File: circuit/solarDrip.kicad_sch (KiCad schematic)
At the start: 44 parts, among them J1 solar_charger, J10 Conn_01x08_Socket, J2 batt, J3 solar, J4 pump, J5 soil, J6 water, J7 USB_C_Receptacle_USB2.0_14P, J8 i2c, J9 Conn_01x08_Socket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

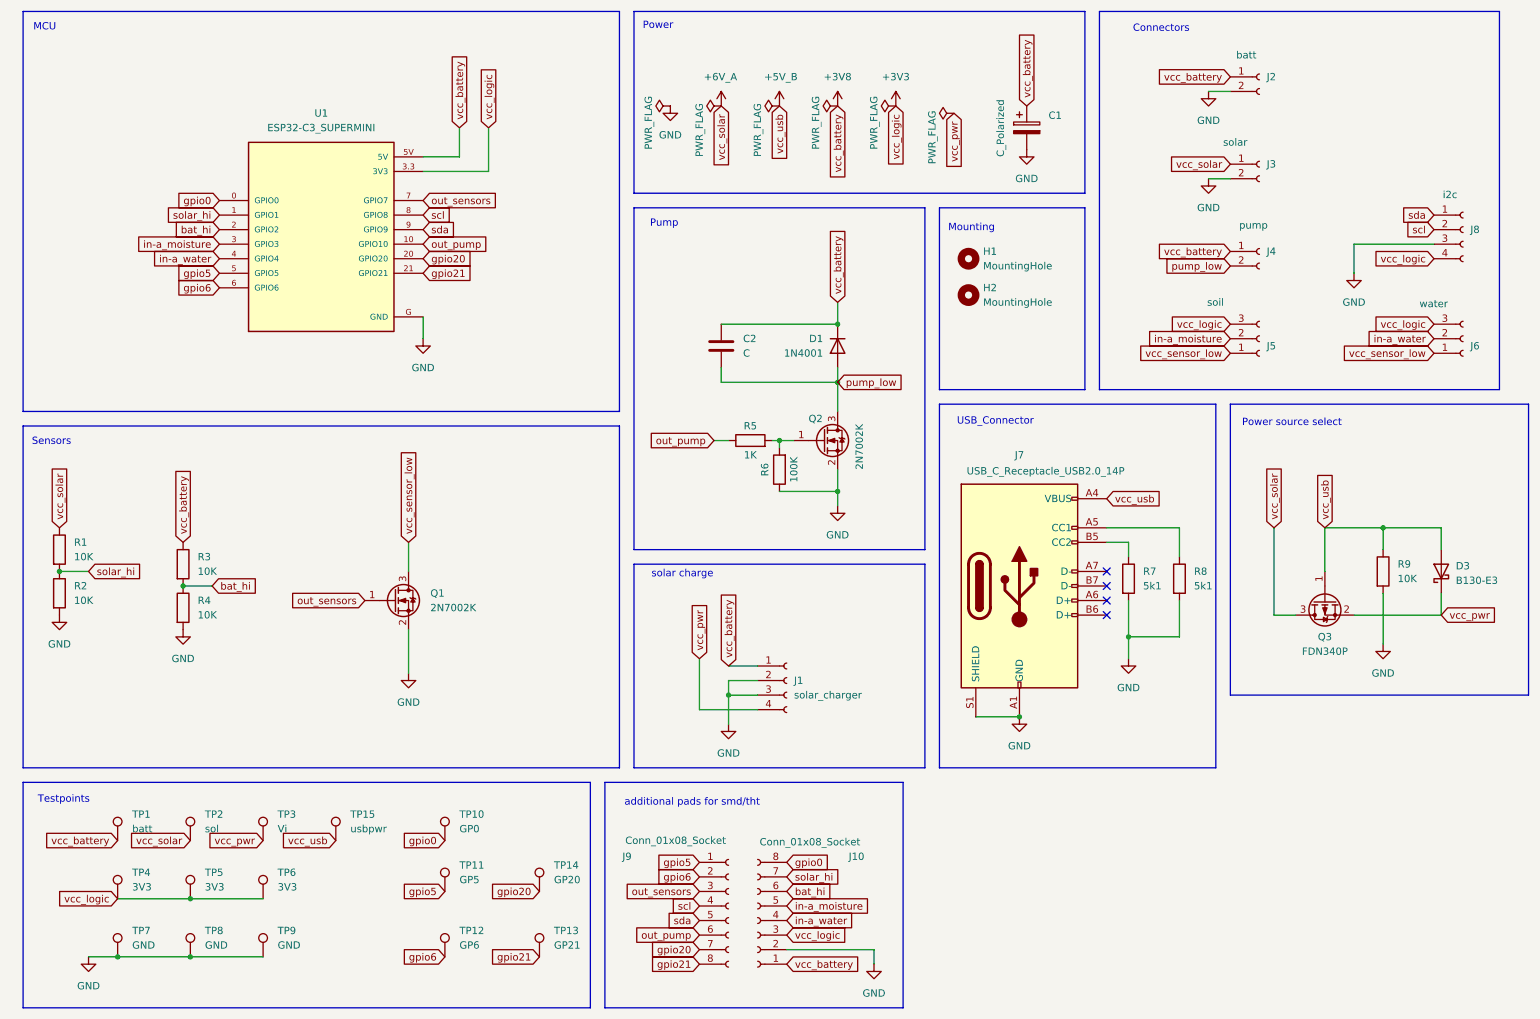
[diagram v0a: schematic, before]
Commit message: sch: add bypass caps to sensor pins
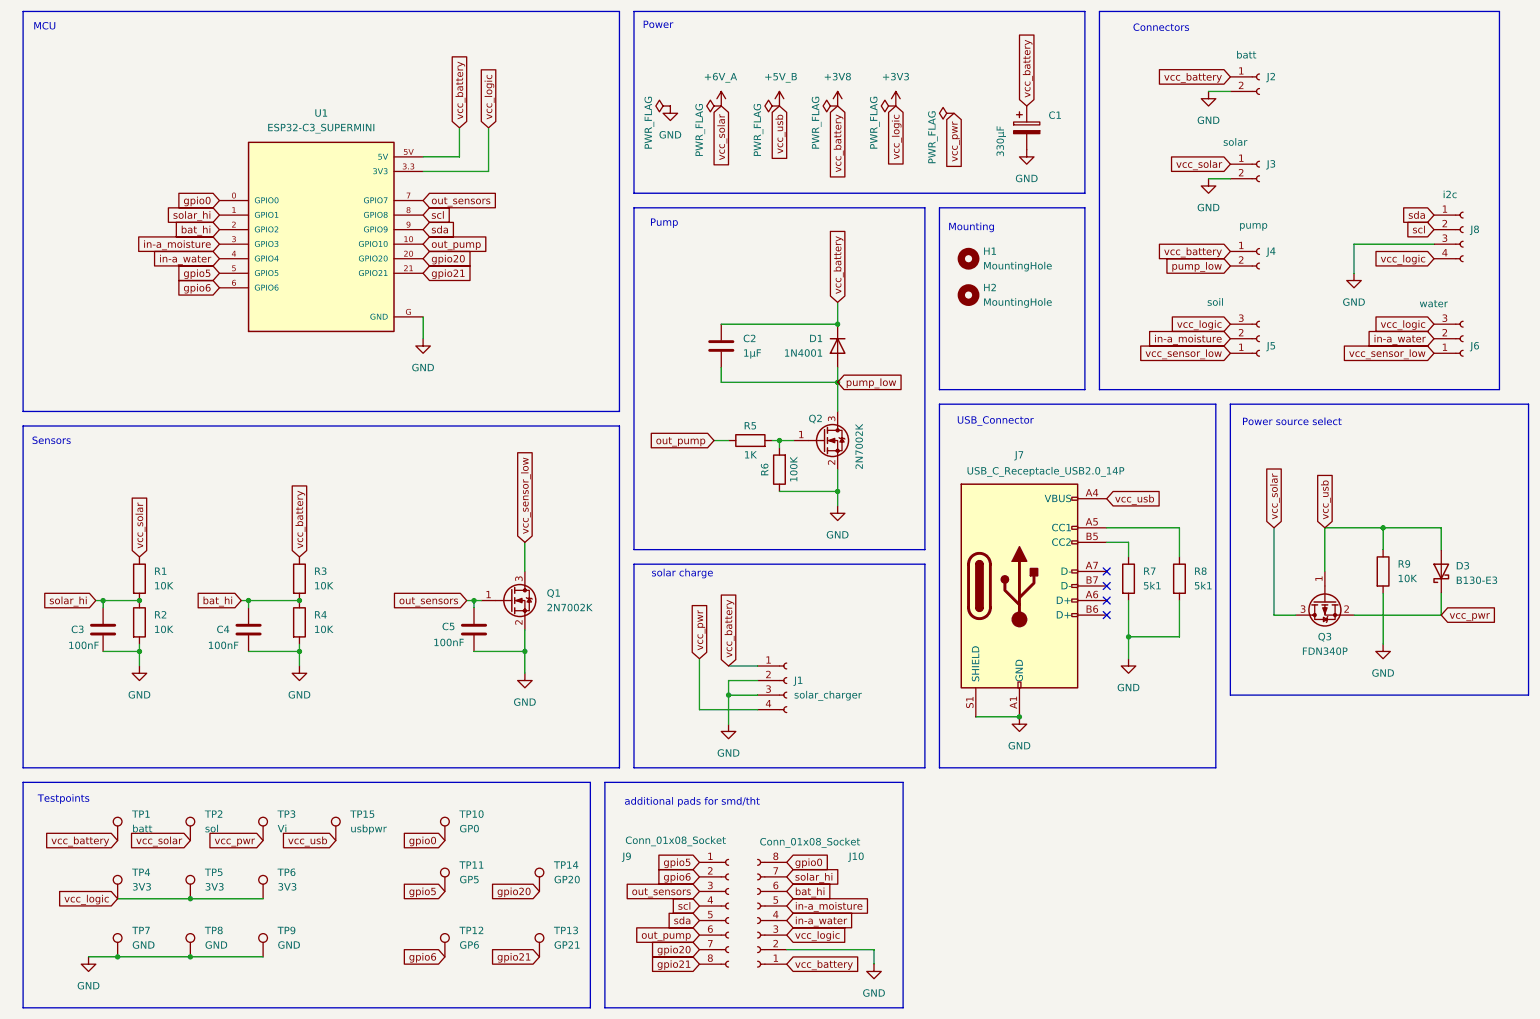
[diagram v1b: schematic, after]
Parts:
- added C3, C4, C5: 100nF, Capacitor_SMD:C_0504_1310Metric_Pad0.83x1.28mm_HandSolder, symbol Device:C
- C1: value C_Polarized -> 330µF
- C2: value C -> 1µF
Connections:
- net GND: now also C3.2, C4.2, C5.2
- net bat_hi: now also C4.1
- net out_sensors: now also C5.1
- net solar_hi: now also C3.1
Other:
- moved on the sheet: Q1, R1, R2, R3, R4

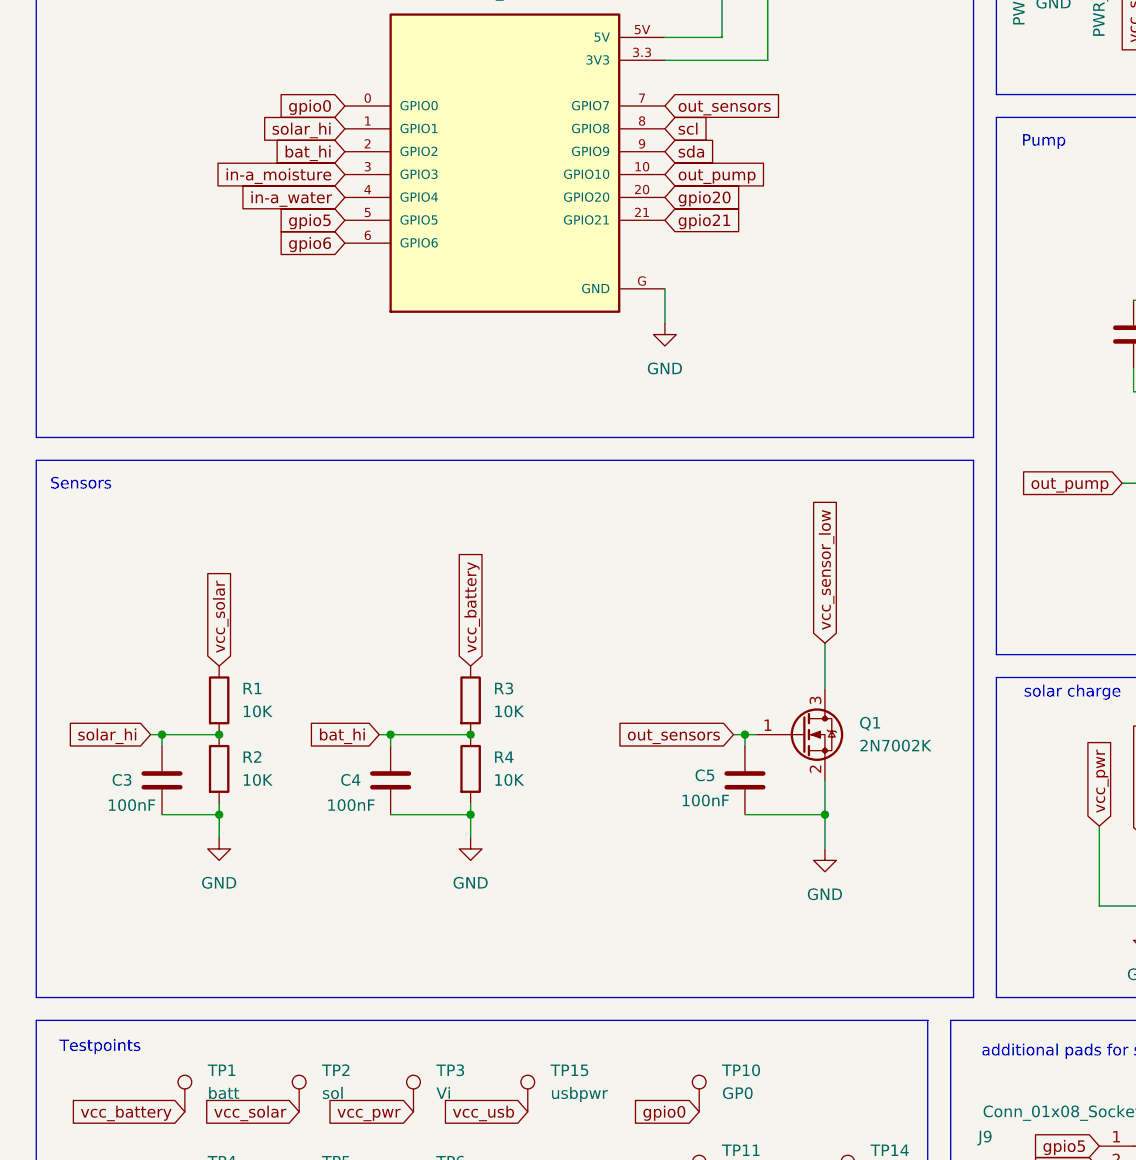
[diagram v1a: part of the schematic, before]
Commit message: add sensor pypass caps
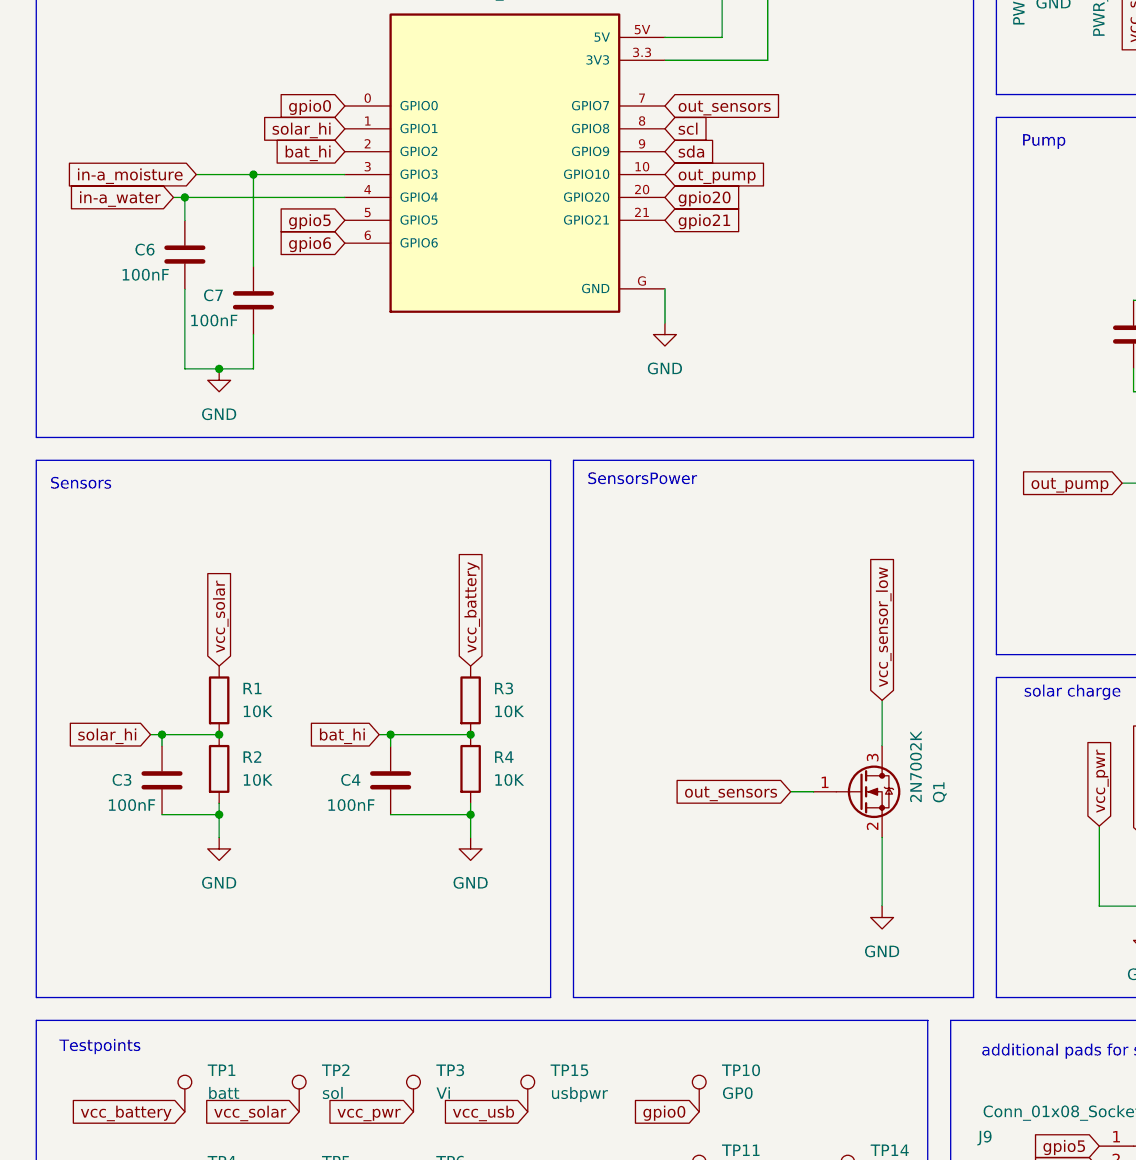
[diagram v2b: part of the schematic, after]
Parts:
- removed C5: 100nF, Capacitor_SMD:C_0504_1310Metric_Pad0.83x1.28mm_HandSolder, symbol Device:C
- added C6, C7: 100nF, Capacitor_SMD:C_0504_1310Metric_Pad0.83x1.28mm_HandSolder, symbol Device:C
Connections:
- net GND: now also C6.2, C7.2
- net in-a_moisture: now also C7.1
- net in-a_water: now also C6.1
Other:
- note added: "SensorsPower"
- moved on the sheet: Q1

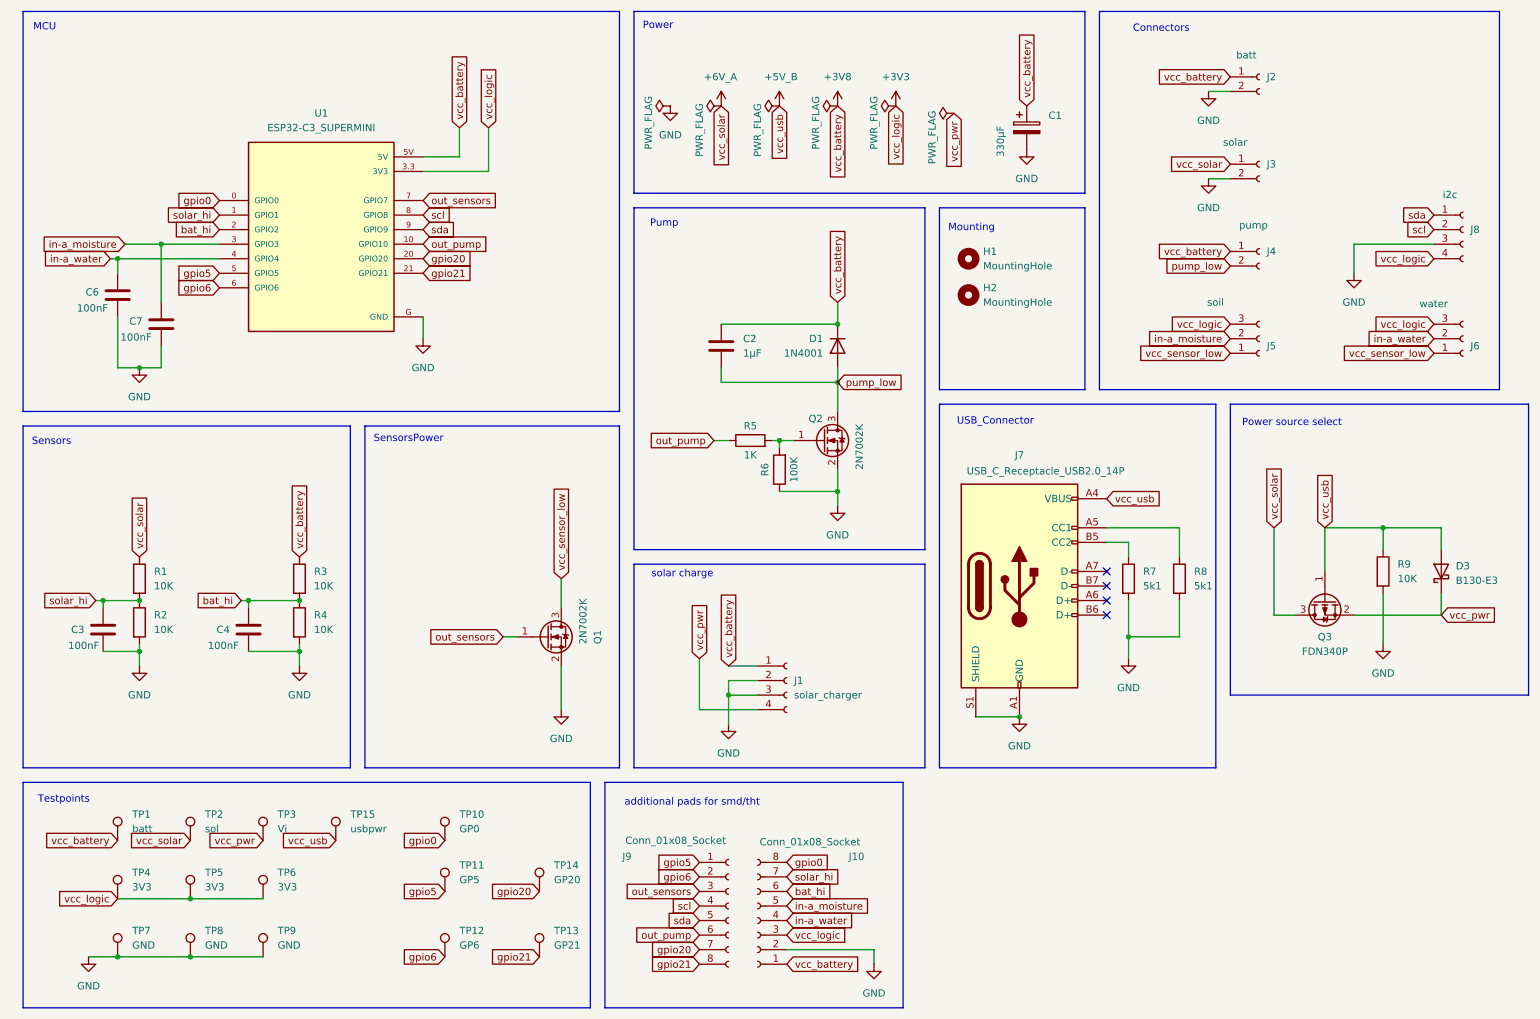
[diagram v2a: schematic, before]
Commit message: add artwork: dripbot & mc3 logo
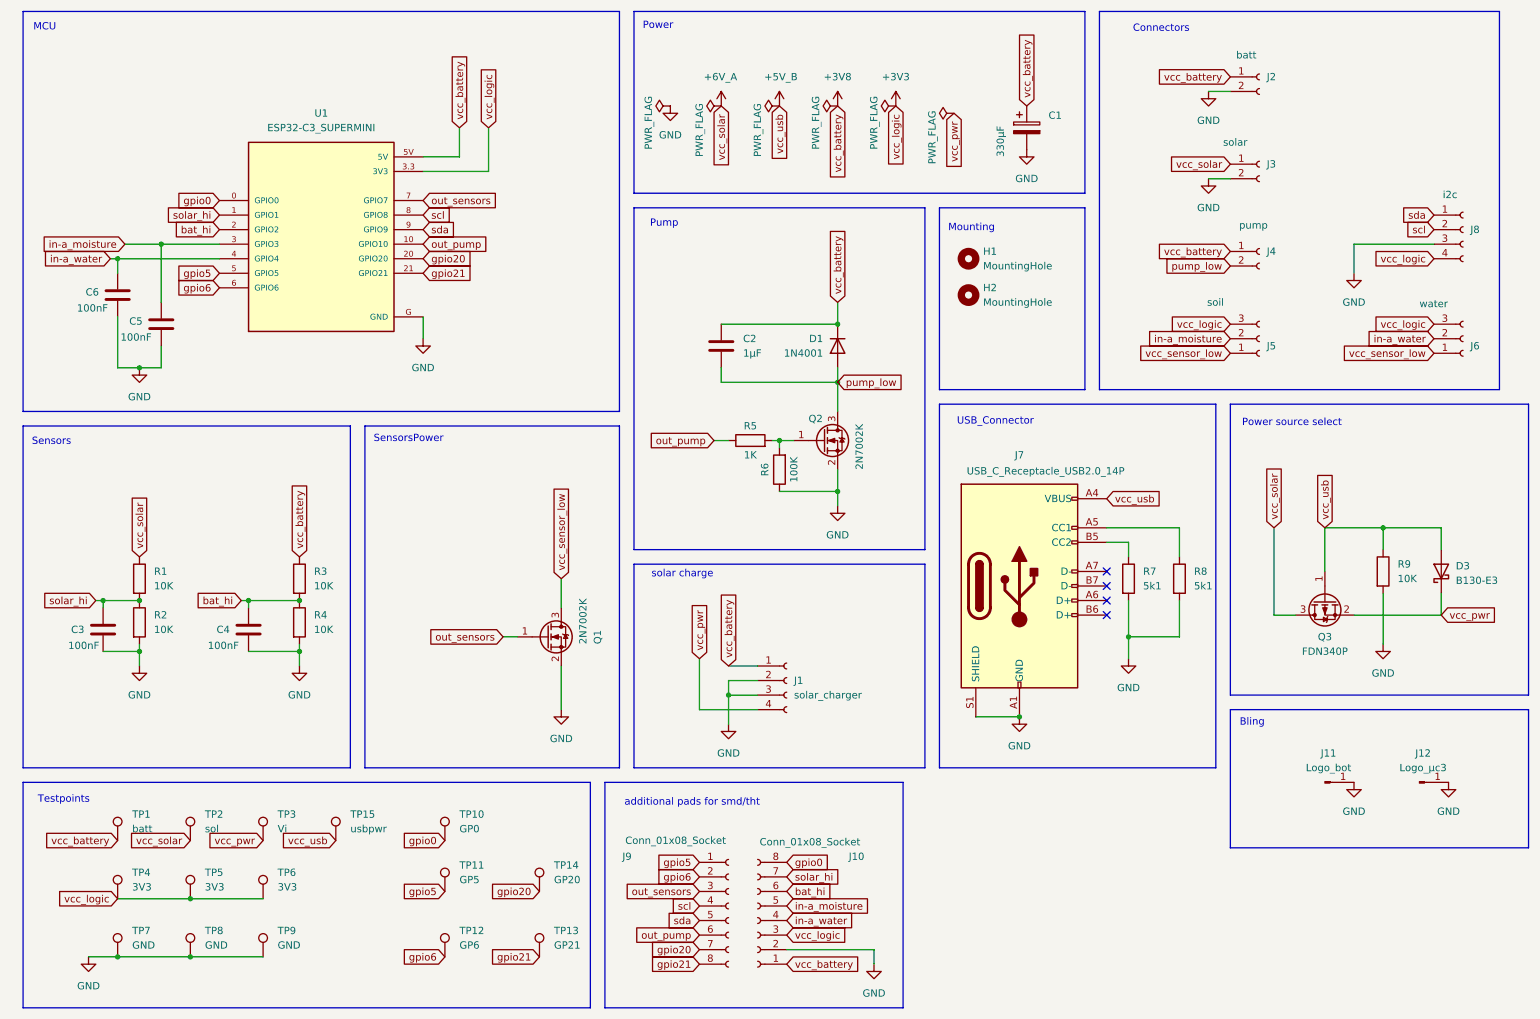
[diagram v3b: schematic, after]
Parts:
- added J11: Logo_bot, my_footprints:logo_solardrip, symbol Connector:Conn_01x01_Pin
- added J12: Logo_µc3, my_footprints:muccc_logo, symbol Connector:Conn_01x01_Pin
- renumbered C7 to C5
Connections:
- net GND: now also J11.1 (Pin_1), J12.1 (Pin_1)
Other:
- note added: "Bling"

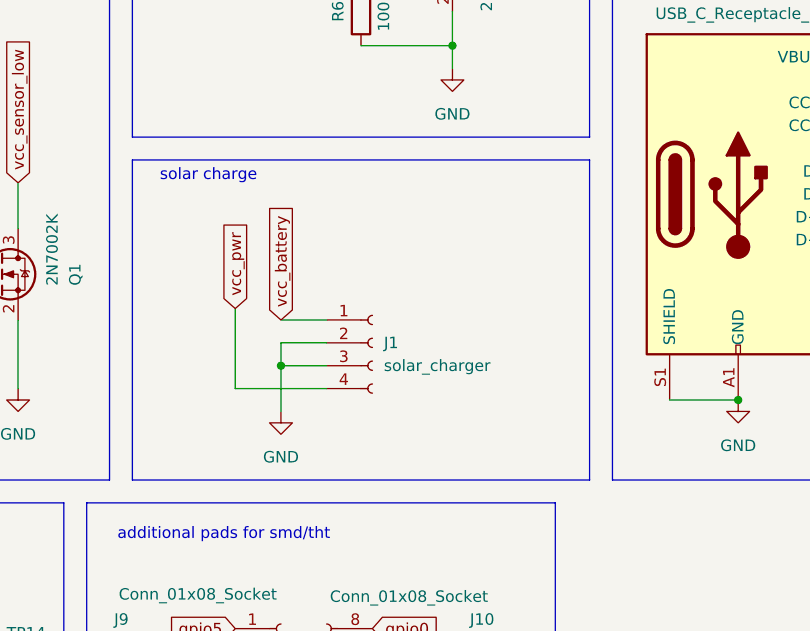
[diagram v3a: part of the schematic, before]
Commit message: add knockout fonts
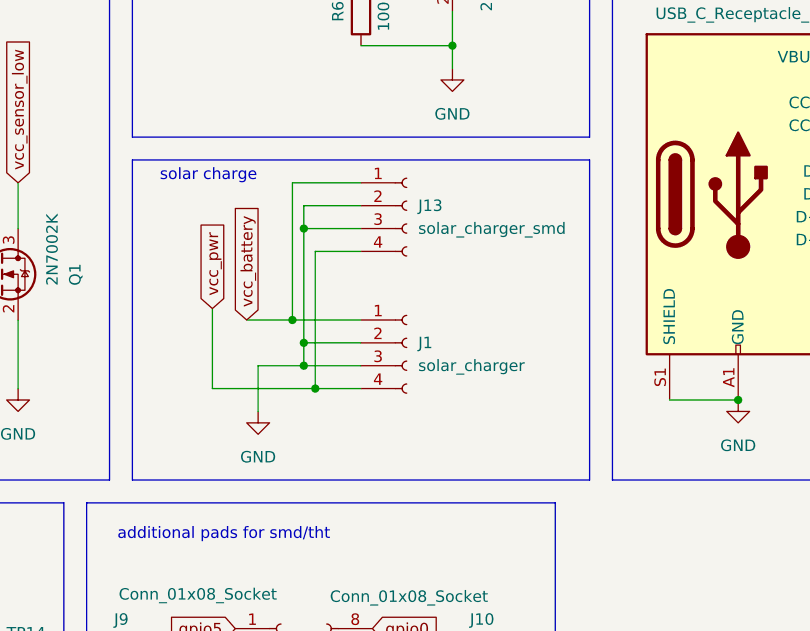
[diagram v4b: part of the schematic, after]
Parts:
- added J13: solar_charger_smd, Connector_PinSocket_2.54mm:PinSocket_1x04_P2.54mm_Vertical_SMD_Pin1Left, symbol Connector:Conn_01x04_Socket
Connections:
- net +3V8: now also J13.1 (Pin_1)
- net GND: now also J13.2 (Pin_2), J13.3 (Pin_3)
- net vcc_pwr: now also J13.4 (Pin_4)
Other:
- moved on the sheet: J1
